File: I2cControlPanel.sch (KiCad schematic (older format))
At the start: 55 parts, among them J1 Conn_01x08, J2 Conn_01x06, J3 Conn_01x04, J4 Conn_01x04, J5 Conn_01x08, J6 Conn_01x04, SW0 SW_Push, SW1 SW_Push, SW2 SW_Push, SW3 SW_Push, SW4 SlideSwitch, SW5 SlideSwitch, SW6 SW_Push, U1 NJM12888F33, U2 ATmega328PB-MU, U3 AQM0802

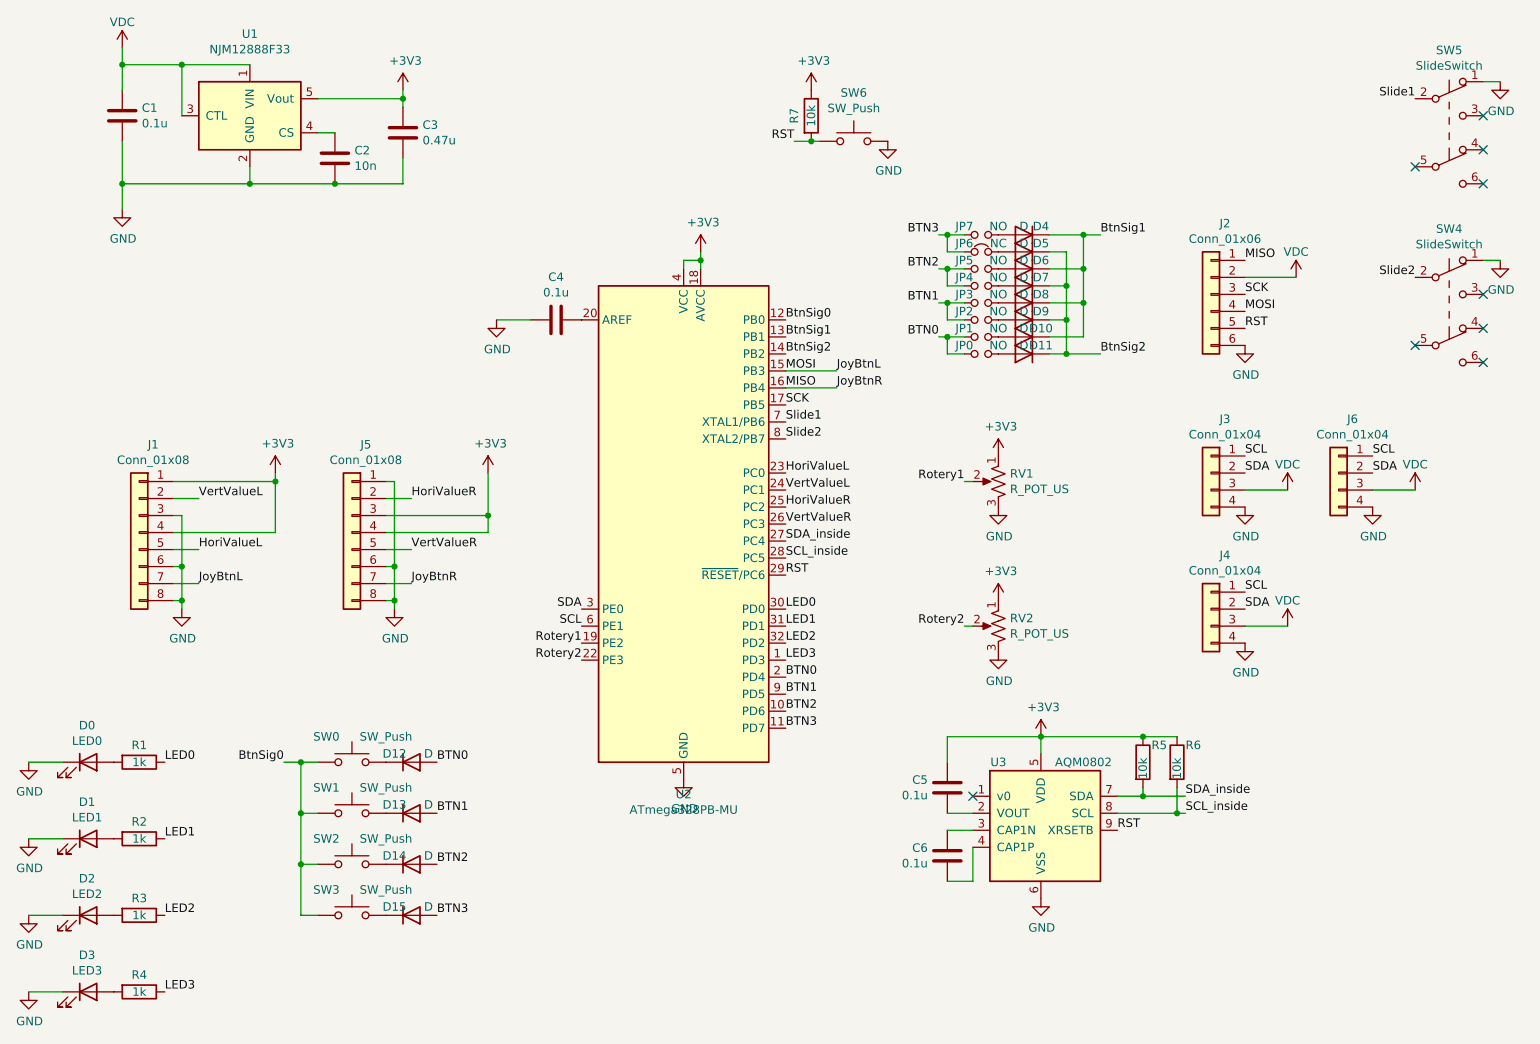
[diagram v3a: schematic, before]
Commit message: Update slide switch position and labels for each buttons
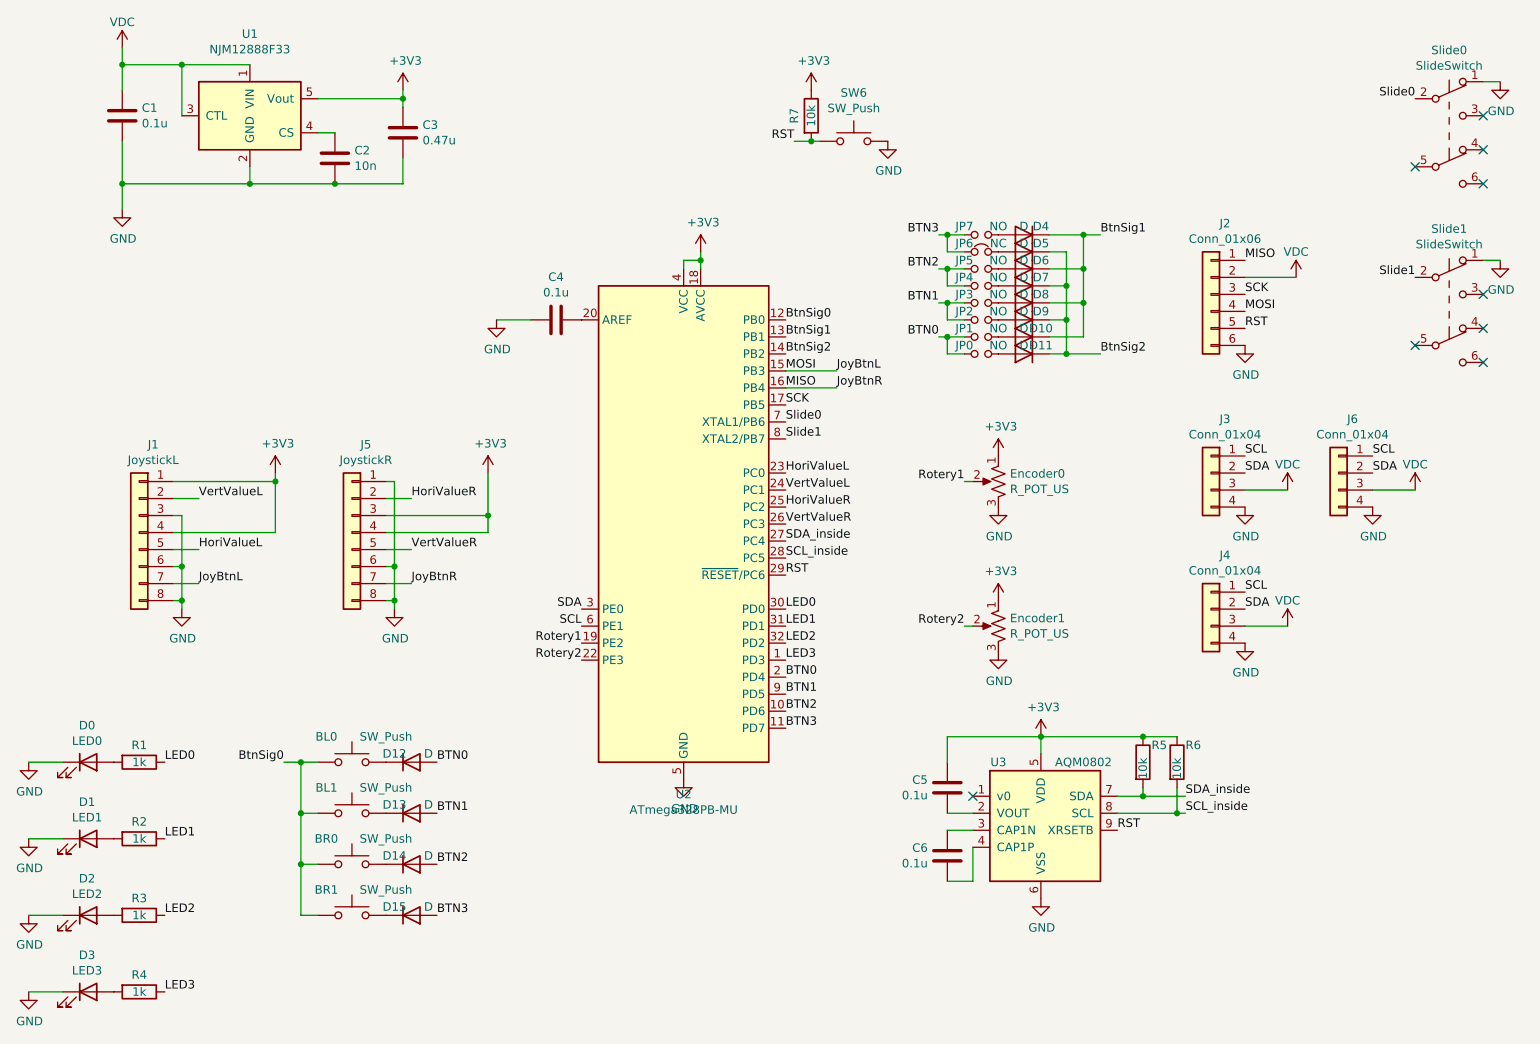
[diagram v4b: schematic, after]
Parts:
- J1: value Conn_01x08 -> JoystickL
- J5: value Conn_01x08 -> JoystickR
- renumbered SW0 to BL0, SW1 to BL1, SW2 to BR0, SW3 to BR1, RV1 to Encoder0, RV2 to Encoder1, SW5 to Slide0, SW4 to Slide1
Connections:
- net Slide2 is gone; now on net Slide1: Slide1.2 (B), U2.8 (XTAL2/PB7)
- net Slide1: no longer Slide0.2 (B), U2.7 (XTAL1/PB6)
- new net Slide0: Slide0.2 (B), U2.7 (XTAL1/PB6)
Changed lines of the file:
@@
 $EndComp
 $Comp
-L Switch:SW_Push SW0
+L Switch:SW_Push BL0
 U 1 1 5D2E3CD5
 P 3900 5200
-F 0 "SW0" H 3750 5350 50  0000 C CNN
+F 0 "BL0" H 3750 5350 50  0000 C CNN
 F 1 "SW_Push" H 4100 5350 50  0000 C CNN
 F 2 "footprints:SW_Center_PUSH-12mm" H 3900 5400 50  0001 C CNN
@@
 BTN1
 $Comp
-L Switch:SW_Push SW1
+L Switch:SW_Push BL1
 U 1 1 5D36B867
 P 3900 5500
-F 0 "SW1" H 3750 5650 50  0000 C CNN
+F 0 "BL1" H 3750 5650 50  0000 C CNN
 F 1 "SW_Push" H 4100 5650 50  0000 C CNN
 F 2 "footprints:SW_Center_PUSH-12mm" H 3900 5700 50  0001 C CNN
@@
 $EndComp
 $Comp
-L Switch:SW_Push SW2
+L Switch:SW_Push BR0
 U 1 1 5D36D8B0
 P 3900 5800
-F 0 "SW2" H 3750 5950 50  0000 C CNN
+F 0 "BR0" H 3750 5950 50  0000 C CNN
 F 1 "SW_Push" H 4100 5950 50  0000 C CNN
 F 2 "footprints:SW_Center_PUSH-12mm" H 3900 6000 50  0001 C CNN
@@
 $EndComp
 $Comp
-L Switch:SW_Push SW3
+L Switch:SW_Push BR1
 U 1 1 5D371214
 P 3900 6100
-F 0 "SW3" H 3750 6250 50  0000 C CNN
+F 0 "BR1" H 3750 6250 50  0000 C CNN
 F 1 "SW_Push" H 4100 6250 50  0000 C CNN
 F 2 "footprints:SW_Center_PUSH-12mm" H 3900 6300 50  0001 C CNN
@@
 $EndComp
 $Comp
-L Device:R_POT_US RV1
+L Device:R_POT_US Encoder0
 U 1 1 5EE7F6DB
 P 7700 3550
-F 0 "RV1" H 7632 3596 50  0000 R CNN
+F 0 "Encoder0" H 7632 3596 50  0000 R CNN
 F 1 "R_POT_US" H 7632 3505 50  0000 R CNN
 F 2 "my-kicad-footprints:Volume" H 7700 3550 50  0001 C CNN
@@
 	7500 3550 7550 3550
 $Comp
-L Device:R_POT_US RV2
+L Device:R_POT_US Encoder1
 U 1 1 5EE88740
 P 7700 4400
-F 0 "RV2" H 7632 4446 50  0000 R CNN
+F 0 "Encoder1" H 7632 4446 50  0000 R CNN
 F 1 "R_POT_US" H 7632 4355 50  0000 R CNN
 F 2 "my-kicad-footprints:Volume" H 7700 4400 50  0001 C CNN
@@
 P 2650 3850
 F 0 "J1" H 2568 4367 50  0000 C CNN
-F 1 "Conn_01x08" H 2568 4276 50  0000 C CNN
+F 1 "JoystickL" H 2568 4276 50  0000 C CNN
 F 2 "my-kicad-footprints:LowHeightJoyStickWithButton" H 2650 3850 50  0001 C CNN
 F 3 "~" H 2650 3850 50  0001 C CNN
@@
 P 3900 3850
 F 0 "J5" H 3818 4367 50  0000 C CNN
-F 1 "Conn_01x08" H 3818 4276 50  0000 C CNN
+F 1 "JoystickR" H 3818 4276 50  0000 C CNN
 F 2 "my-kicad-footprints:LowHeightJoyStickWithButton" H 3900 3850 50  0001 C CNN
 F 3 "~" H 3900 3850 50  0001 C CNN
@@
 	3600 5500 3600 5800
 Text Label 6450 3200 0    50   ~ 0
+Slide0
+Text Label 6450 3300 0    50   ~ 0
 Slide1
-Text Label 6450 3300 0    50   ~ 0
-Slide2
 NoConn ~ 10550 1800
 Text Label 6450 4600 0    50   ~ 0
@@
 NoConn ~ 10550 1600
 Text Label 10150 1300 2    50   ~ 0
-Slide1
+Slide0
 $Comp
 L power:GND #PWR0117
@@
 $EndComp
 $Comp
-L Switch:SW_Push_DPDT SW5
+L Switch:SW_Push_DPDT Slide0
 U 1 1 5EEC5D06
 P 10350 1500
-F 0 "SW5" H 10350 1985 50  0000 C CNN
+F 0 "Slide0" H 10350 1985 50  0000 C CNN
 F 1 "SlideSwitch" H 10350 1894 50  0000 C CNN
 F 2 "my-kicad-footprints:SlideSwitch" H 10350 1700 50  0001 C CNN
@@
 NoConn ~ 10550 2650
 Text Label 10150 2350 2    50   ~ 0
-Slide2
+Slide1
 $Comp
 L power:GND #PWR0119
@@
 $EndComp
 $Comp
-L Switch:SW_Push_DPDT SW4
+L Switch:SW_Push_DPDT Slide1
 U 1 1 5F41D1BB
 P 10350 2550
-F 0 "SW4" H 10350 3035 50  0000 C CNN
+F 0 "Slide1" H 10350 3035 50  0000 C CNN
 F 1 "SlideSwitch" H 10350 2944 50  0000 C CNN
 F 2 "my-kicad-footprints:SlideSwitch" H 10350 2750 50  0001 C CNN
